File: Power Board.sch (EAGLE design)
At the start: 36 parts, among them IC1 SN74LS00N, Q1 IRLB8743PBF, U1 S18V20F12, U2 D24V22F3, U3 D24V22F5

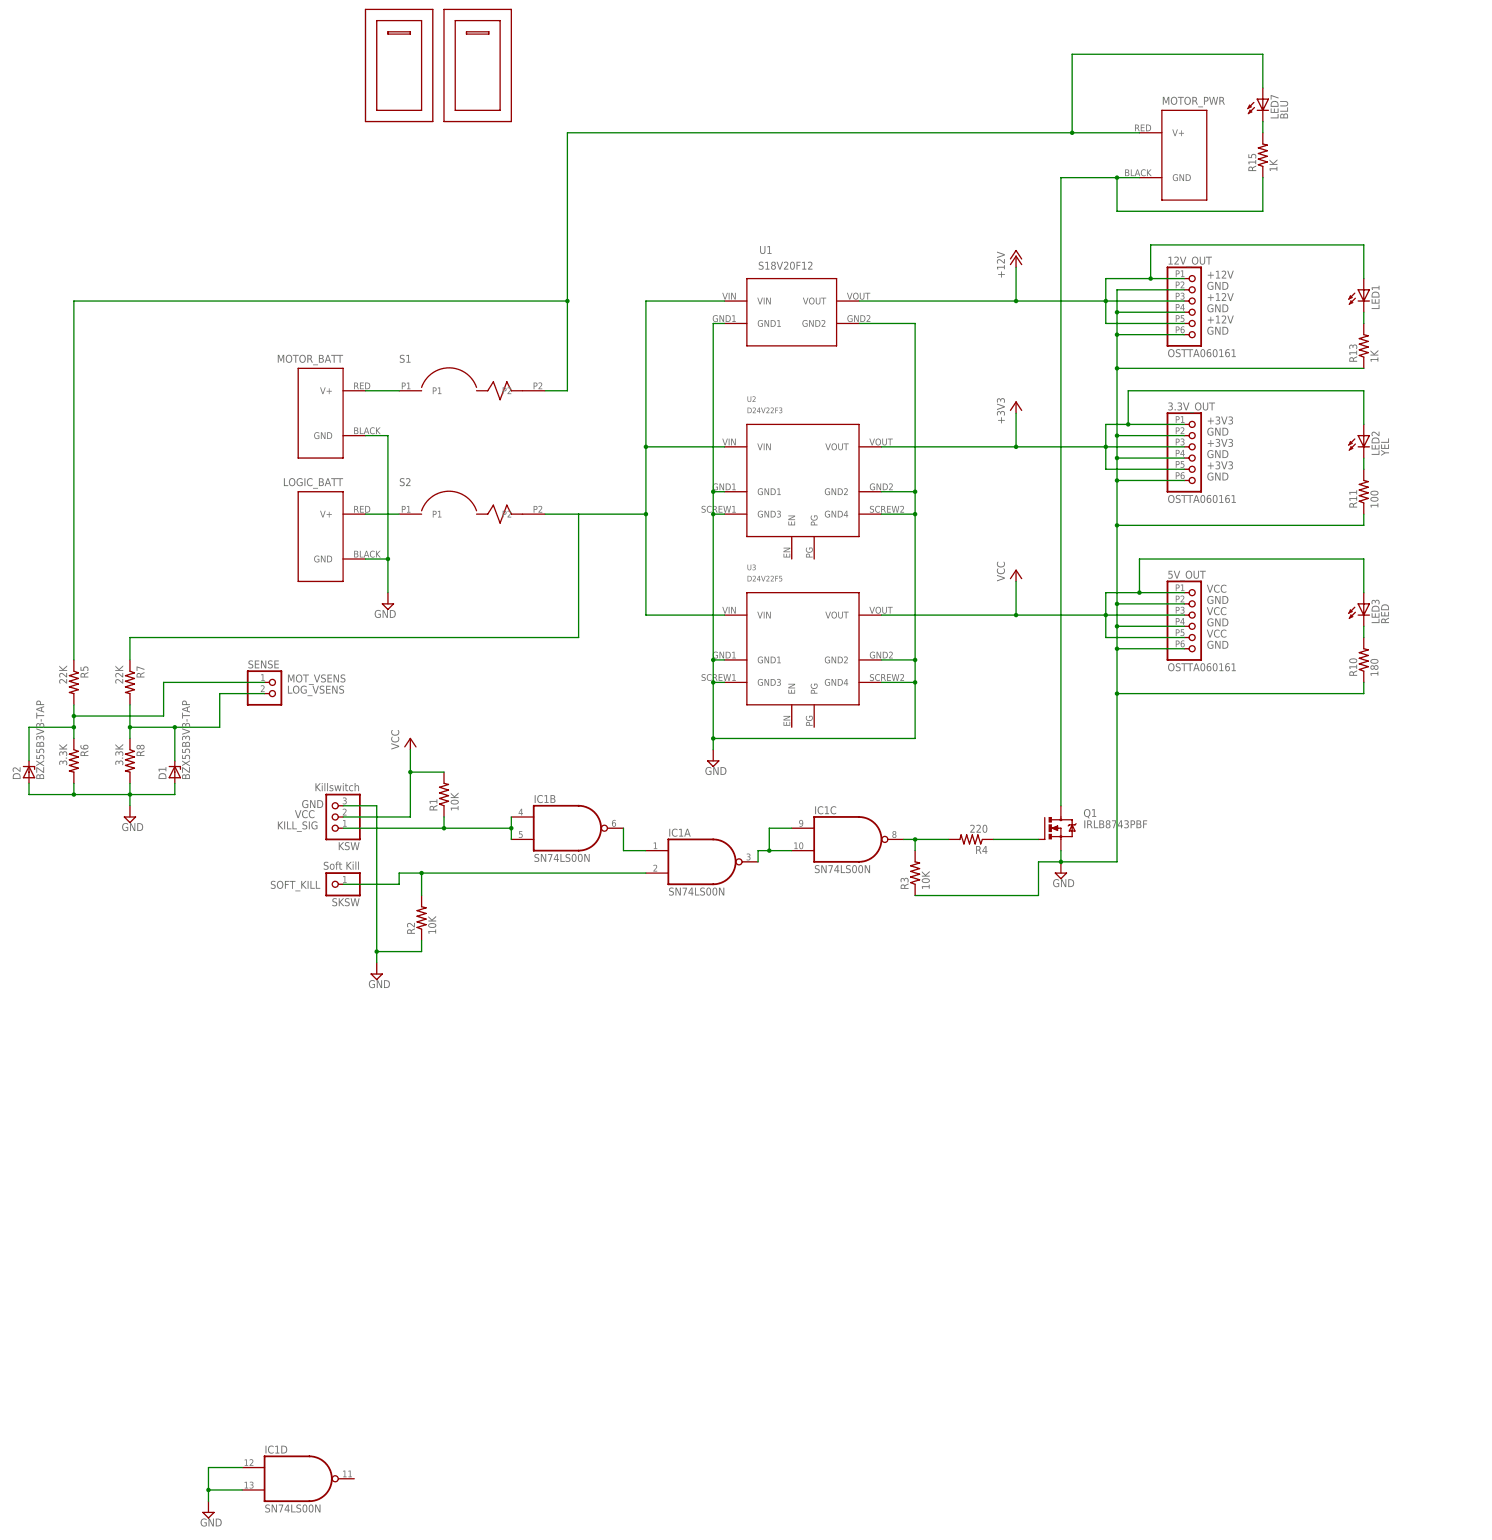
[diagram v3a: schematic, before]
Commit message: Start on new SMD version of power board -- add LTC FET driver, convert NAND gate to SMD
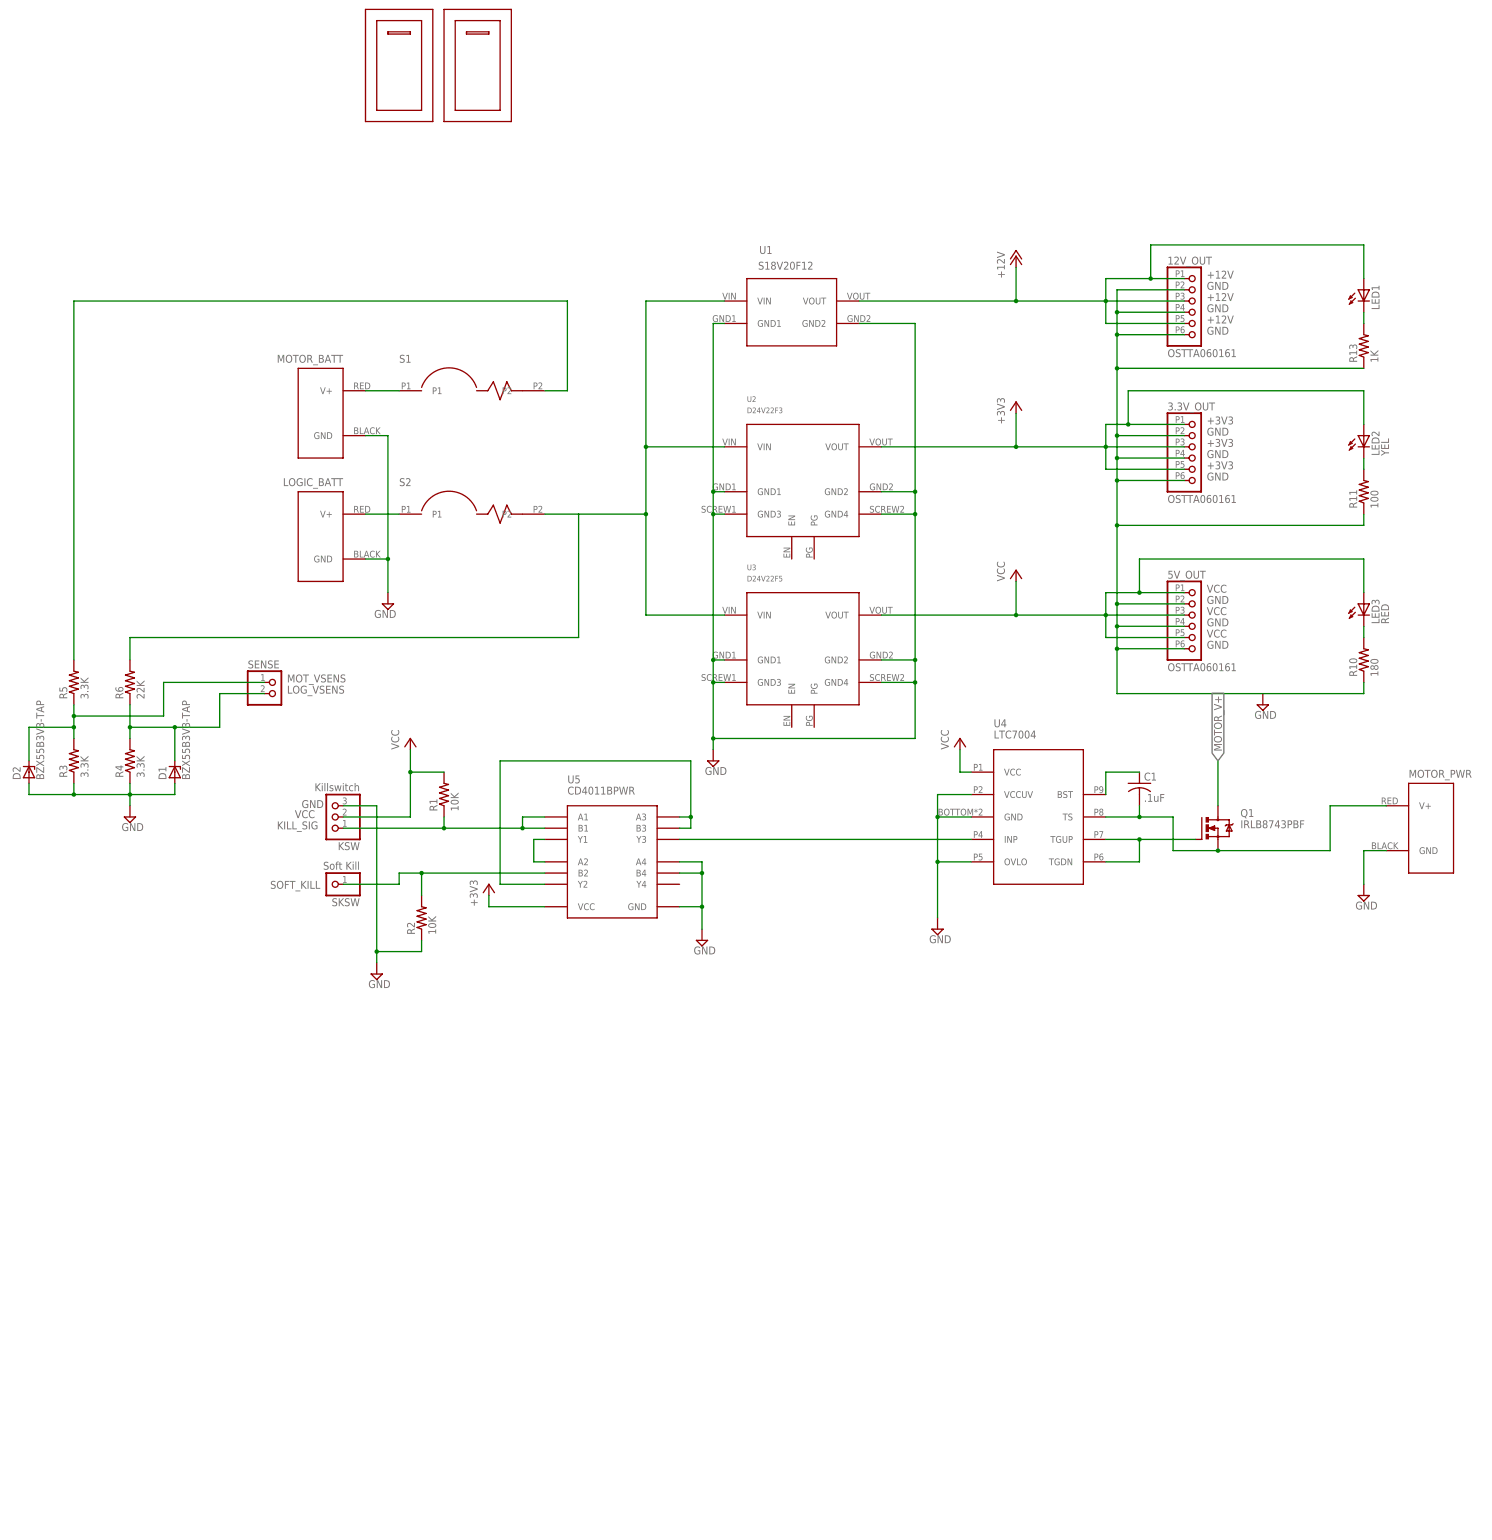
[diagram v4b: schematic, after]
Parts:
- removed IC1: SN74LS00N, 74xx-us:74LS00N
- removed LED7: BLU, led:LED5MM
- removed R15: 1K, resistor:R-US_0207/10
- removed R7: 22K, resistor:R-US_0207/10
- removed R8: 3.3K, resistor:R-US_0207/10
- added C1: .1uF, rcl:C-USC1206
- added U4: LTC7004, Power Board Custom:LTC7004
- added U5: CD4011BPWR, Power Board Custom:CD4011BPWR
- R3: value 10K -> 3.3K; device resistor:R-US_0207/10 -> rcl:R-US_R1206
- R4: value 220 -> 3.3K; device resistor:R-US_0207/10 -> rcl:R-US_R1206
- R5: value 22K -> 3.3K; device resistor:R-US_0207/10 -> rcl:R-US_R1206
- R6: value 3.3K -> 22K; device resistor:R-US_0207/10 -> rcl:R-US_R1206
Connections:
- removed net MOTOR_0V: MOTOR_PWR.GND, Q1.D, R15.1
- removed net N$1: IC1A.I0, IC1B.O
- removed net N$13: LED7.C, R15.2
- removed net POWER_FET_GATE: Q1.G, R4.1
- new net N$11: C1.1, U4.BST
- new net N$3: U5.A3, U5.B3, U5.Y2
- new net N$8: Q1.G, U4.TGDN, U4.TGUP
- new net N$9: C1.2, MOTOR_PWR.V+, Q1.S, U4.TS
- net +3V3: now also U5.VCC
- net GND: now also MOTOR_PWR.GND, R4.1, U4.GND, U4.OVLO, U4.VCCUV, U5.A4, U5.B4, U5.GND; no longer IC1D.I0, IC1D.I1, Q1.S, R6.2, R8.2
- net KILL_SIG: now also U5.A1, U5.B1; no longer IC1B.I0, IC1B.I1
- net LOG_VIN: now also R6.2; no longer R7.1
- net LOG_VSENS: now also R4.2, R6.1; no longer R7.2, R8.1
- net MOTOR_V+: now also Q1.D, R5.2; no longer LED7.A, MOTOR_PWR.V+, R5.1
- net MOT_VSENS: now also R3.2, R5.1; no longer R5.2, R6.1
- net N$2: now also U5.A2, U5.Y1; no longer IC1A.O, IC1C.I0, IC1C.I1
- net N$4: now also U4.INP, U5.Y3; no longer IC1C.O, R3.2, R4.2
- net SOFT_KILL: now also U5.B2; no longer IC1A.I1
- net VCC: now also U4.VCC
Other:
- moved on the sheet: MOTOR_PWR, Q1, R3, R4, R5, R6

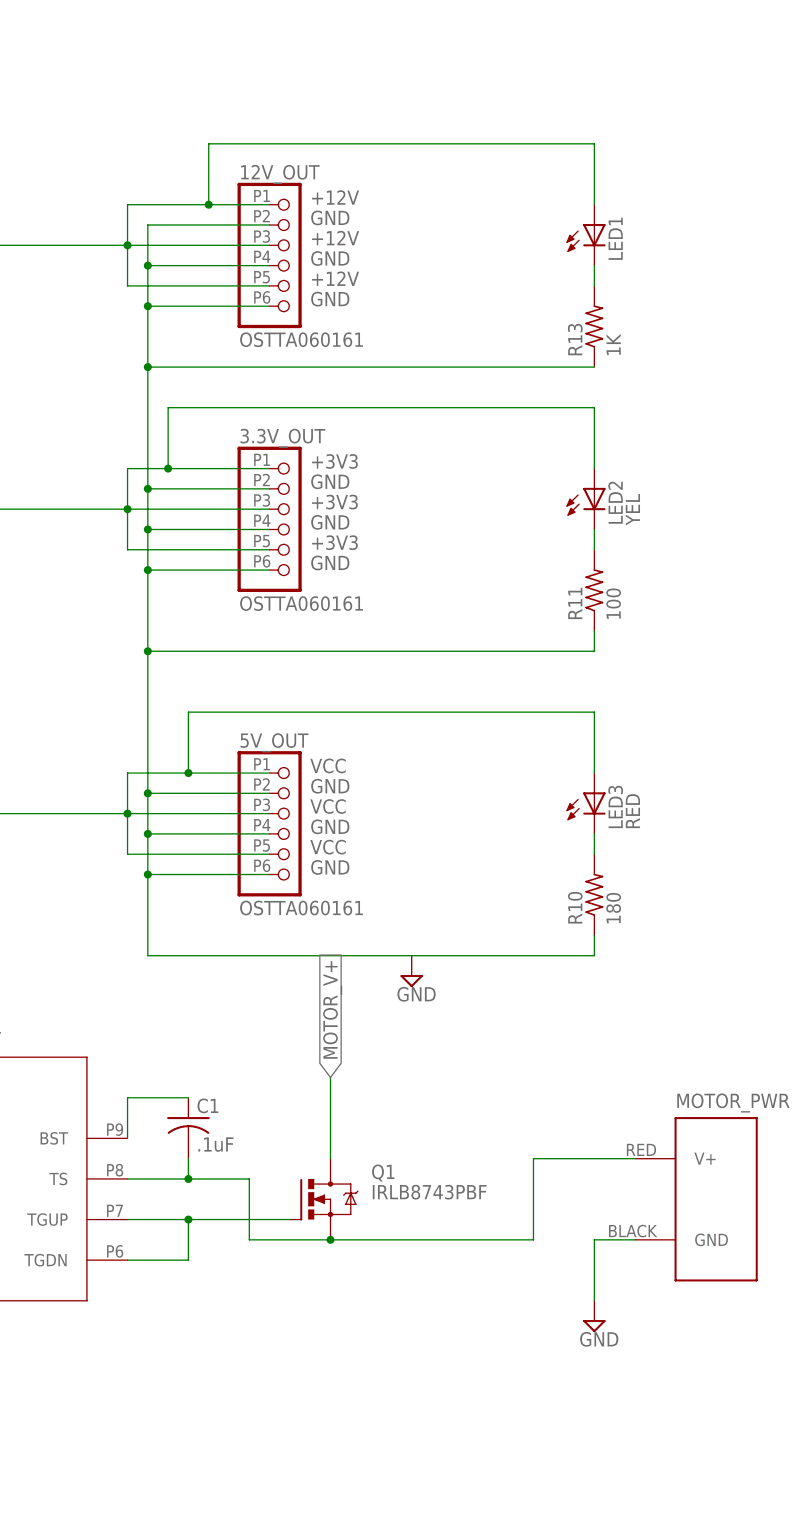
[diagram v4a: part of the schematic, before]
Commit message: Switch LEDs to surface mount, add LTC MOSFET driver
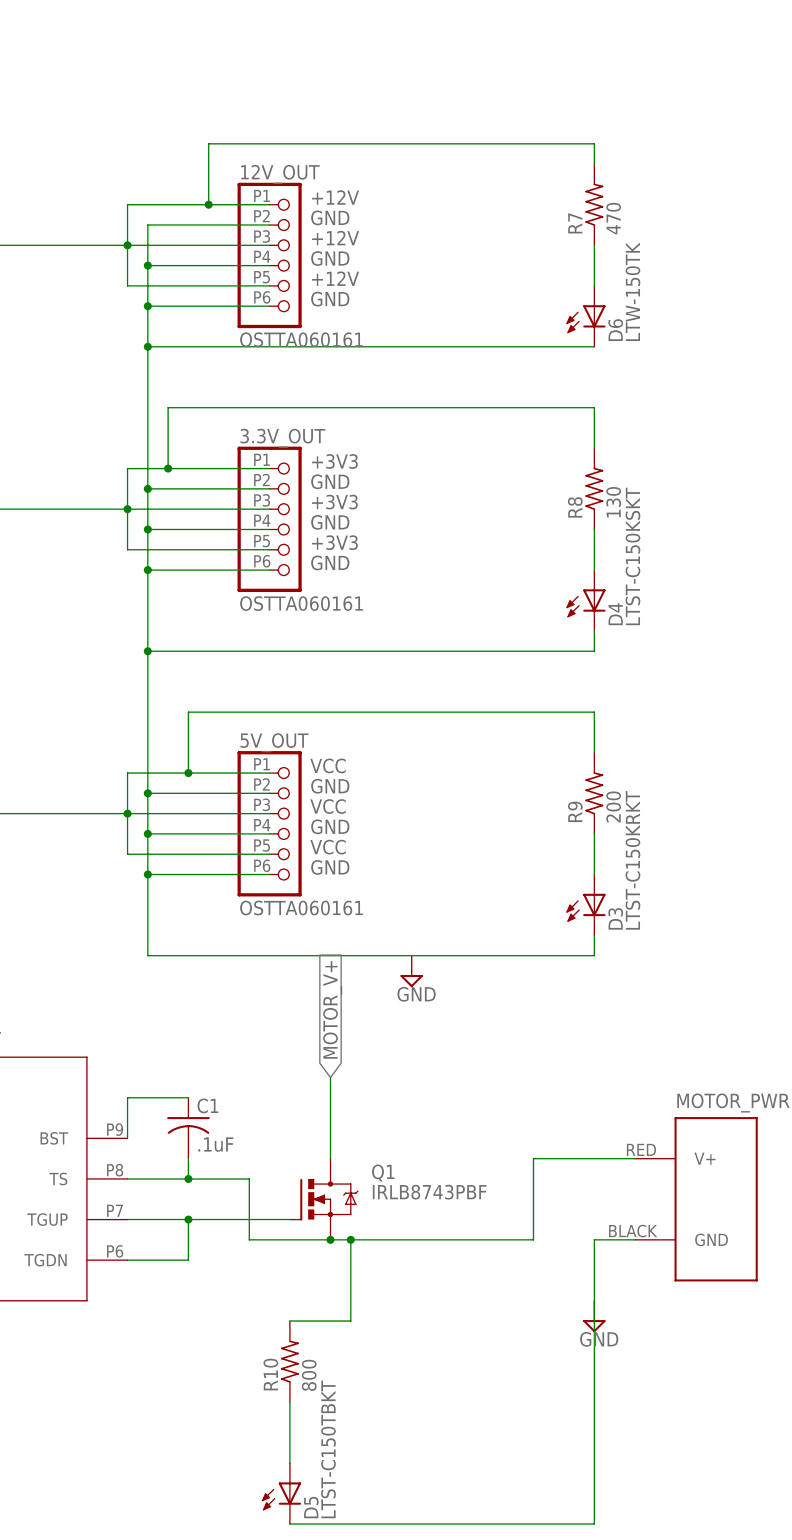
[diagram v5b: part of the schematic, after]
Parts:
- removed LED1: (no value), led:LED5MM
- removed LED2: YEL, led:LED5MM
- removed LED3: RED, led:LED5MM
- removed R11: 100, resistor:R-US_0207/10
- removed R13: 1K, resistor:R-US_0207/10
- added D3: LTST-C150KRKT, Power Board Custom:LTST-C150KRKT
- added D4: LTST-C150KSKT, Power Board Custom:LTST-C150KSKT
- added D5: LTST-C150TBKT, Power Board Custom:LTST-C150TBKT
- added D6: LTW-150TK, Power Board Custom:LTW-150TK
- added R7: 470, rcl:R-US_R1206
- added R8: 130, rcl:R-US_R1206
- added R9: 200, rcl:R-US_R1206
- R10: value 180 -> 800; device resistor:R-US_0207/10 -> rcl:R-US_R1206
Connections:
- removed net N$10: LED1.C, R13.2
- new net N$1: D6.A, R7.1
- new net N$5: D4.A, R8.1
- net +12V: now also R7.2; no longer LED1.A
- net +3V3: now also R8.2; no longer LED2.A
- net GND: now also D3.C, D4.C, D5.C, D6.C; no longer R10.1, R11.1, R13.1
- net N$6: now also D3.A, R9.1; no longer LED3.C, R10.2
- net N$7: now also D5.A, R10.1; no longer LED2.C, R11.2
- net N$9: now also R10.2
- net VCC: now also R9.2; no longer LED3.A
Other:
- moved on the sheet: R10
